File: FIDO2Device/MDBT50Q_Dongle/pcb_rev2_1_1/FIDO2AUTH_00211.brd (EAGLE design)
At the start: 22.9 x 38.7 mm, 35 parts, among them CN1 TE-1734028, CN2 IF_5PIN_H, CN3 IF_3PIN, SW1 SKRPACE010, SW2 SKTADAE010, U1 MDBT50Q-P1M, U2 XC6206P332MR-G, X1 NX3215SA-32.768K

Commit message: 回路図を修正
・ドキュメントタイトル修正、シート追加
・部品の小型化（リセット回路、差動信号回路、LED回路）
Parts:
- C5, C7, C8, C9: device Parts:C0603K -> Parts:C0402
- FB1, FB2, FB3: device Parts:C0402K@1 -> Parts:C0402
- R1, R2, R3, R4, R5, R6: device Parts:R0603 -> Parts:R0402

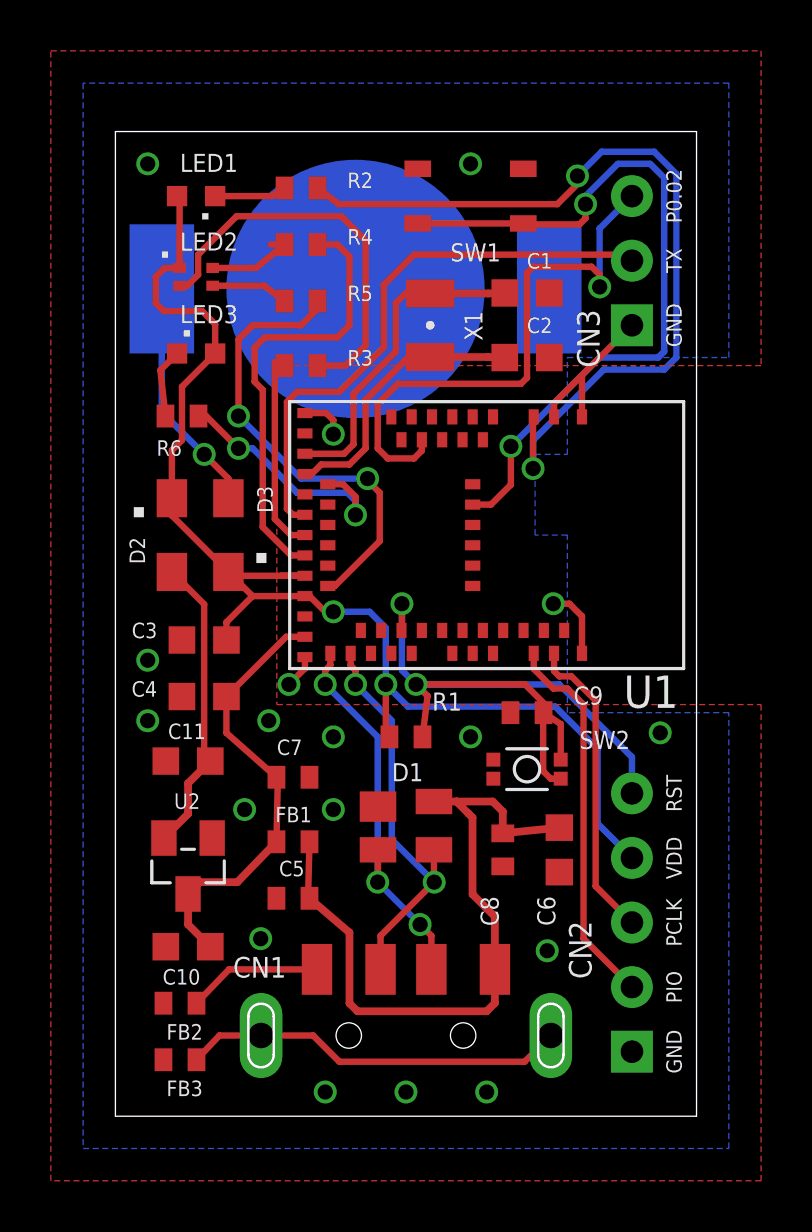
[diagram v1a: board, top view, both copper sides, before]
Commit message: 回路図を修正
・TWI_SDA、TWI_SCLを、実機動作確認結果を元に割り当て
・汎用I/Oを新規に２点割り当て
・プログラム用ピンの配置を修正
（RESETは不要なので廃止、VDDの位置をnRF52840 DK上の順列に合わせる）
・ERC、DRCともにOKを確認
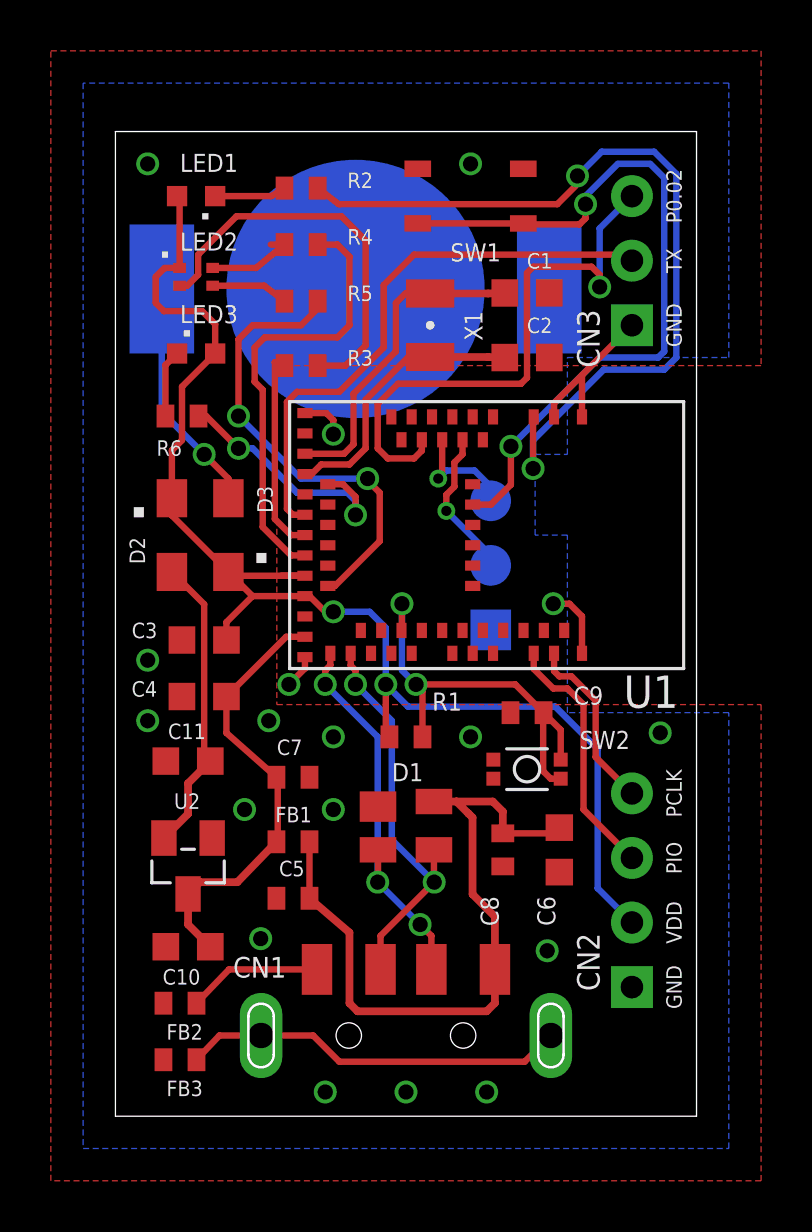
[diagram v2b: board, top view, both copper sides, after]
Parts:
- added CN4: IF_3PIN_SOL, Connectors:SOLPAD_3PIN
- CN2: value IF_5PIN_H -> IF_4PIN; device Connectors:HEADER_5PIN -> Connectors:HEADER_4PIN
- moved CN2 2.54 mm to (20.3, 5.08)
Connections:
- net AIN0 renamed TWI_SCL
- net UART_TX renamed TWI_SDA
- new net P0.03: CN4.3, U1.9
- new net P1.14: CN4.2, U1.7
- net 0V: now also CN4.1
- net RESET: no longer CN2.5
- net SWDCLK: now also CN2.4; no longer CN2.3
- net SWDIO: now also CN2.3; no longer CN2.2
- net VDD_NRF: now also CN2.2; no longer CN2.4
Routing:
- net RESET: track 29.1 -> 17.3 mm
- net P1.14: track 0.00 -> 5.93 mm, vias 0 -> 1
- net SWDIO: track 15.1 -> 9.98 mm
- net SWDCLK: track 12.1 -> 7.06 mm
- net P0.03: track 0.00 -> 4.61 mm, vias 0 -> 1
- net VDD_NRF: track 50.9 -> 53.5 mm
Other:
- board text removed: "RST"

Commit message: プリント基板設計データを修正
・ATECC608Aの配置前に、既存部品のレイアウトを修正
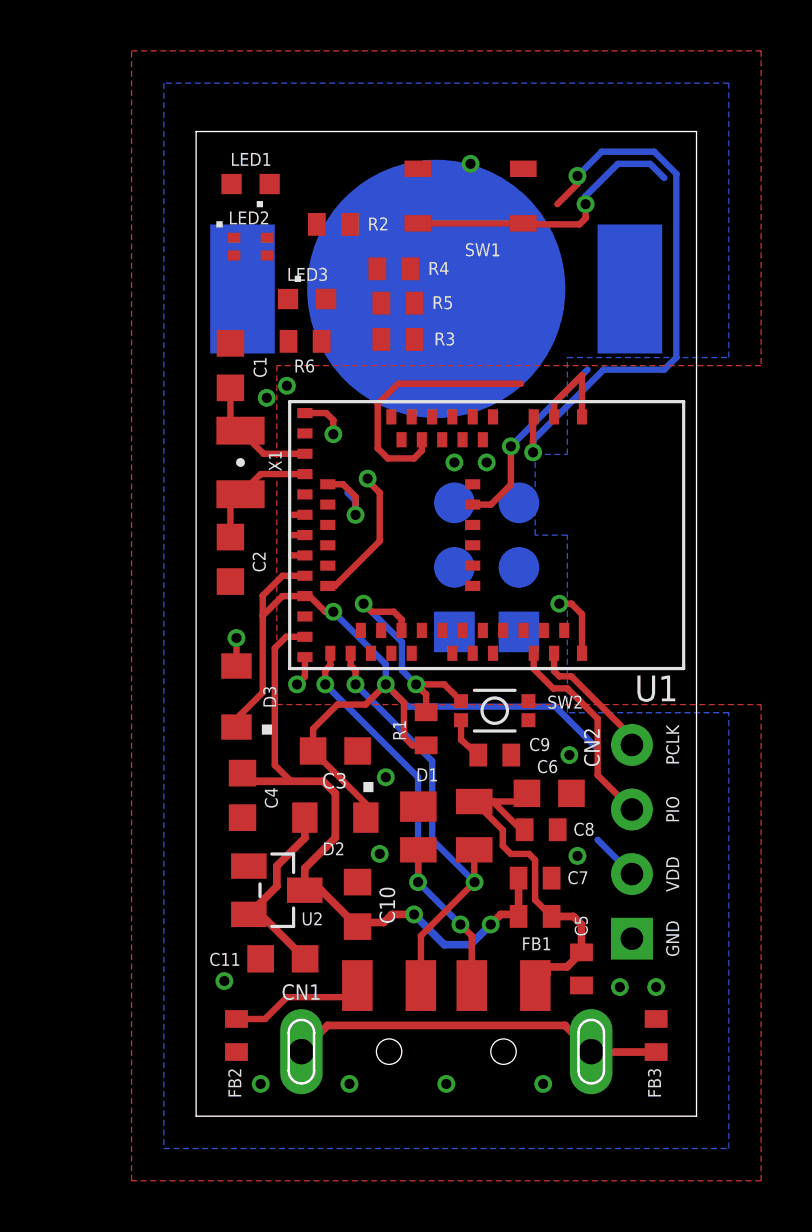
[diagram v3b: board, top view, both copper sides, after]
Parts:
- CN3: value IF_3PIN -> IF_3PIN_SOL; device Connectors:HEADER_3PIN -> Connectors:SOLPAD_3PIN
- moved FB3 18.8 mm to (21.3, 3.17), turned to 90 degrees
- moved C2 14.1 mm to (4.52, 21.9), turned to 270 degrees
- moved CN3 13.9 mm to (13.3, 19.1), flipped to the bottom
- moved D2 12.8 mm to (8.65, 11.7), turned to 180 degrees
- moved C1 12.0 mm to (4.52, 29.5), turned to 90 degrees
- moved C5 11.7 mm to (18.3, 5.79), turned to 270 degrees
- moved C7 10.3 mm to (16.5, 9.37)
- moved FB1 9.97 mm to (16.5, 7.86)
- moved X1 9.21 mm to (4.92, 25.7)
- moved C11 8.63 mm to (6.59, 6.19)
- moved C10 6.87 mm to (9.53, 8.33), turned to 90 degrees
- moved C3 6.76 mm to (8.65, 14.4), turned to 0 degrees
- moved D3 6.36 mm to (4.76, 16.5)
- moved R6 5.66 mm to (7.46, 30.5)
- moved LED3 4.86 mm to (7.54, 32.1)
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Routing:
- net TWI_SDA: track 22.5 -> 0.48 mm
- net LED2_G: track 17.6 -> 0.54 mm
- net VDD_NRF: track 53.5 -> 37.2 mm
- net N$1: track 15.7 -> 0.00 mm
- net LED2_B: track 18.7 -> 5.43 mm
- net VBUS: track 28.2 -> 15.8 mm
- net TWI_SCL: track 22.3 -> 10.2 mm, vias 1 -> 0
- net LED1: track 33.1 -> 22.2 mm
- net SW1: track 29.2 -> 19.0 mm
- net VBUS_NRF: track 17.5 -> 26.9 mm, vias 0 -> 2
- net N$5: track 9.32 -> 0.86 mm
- net XL1: track 12.8 -> 4.76 mm
- net LED2_R: track 8.02 -> 0.55 mm
- net LED3: track 10.1 -> 3.01 mm
- net XL2: track 10.9 -> 4.71 mm
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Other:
- board size 22.9 x 38.7 mm -> 19.7 x 38.7 mm
- board text removed: "P0.02"
- board text removed: "TX"

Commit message: プリント基板設計データを修正
・ATECC608Aの配置前の段階まで配線
・汎用I/Oを P0.25、P1.02 に変更
・TWI_SDA、TWI_SCL は表面に配置
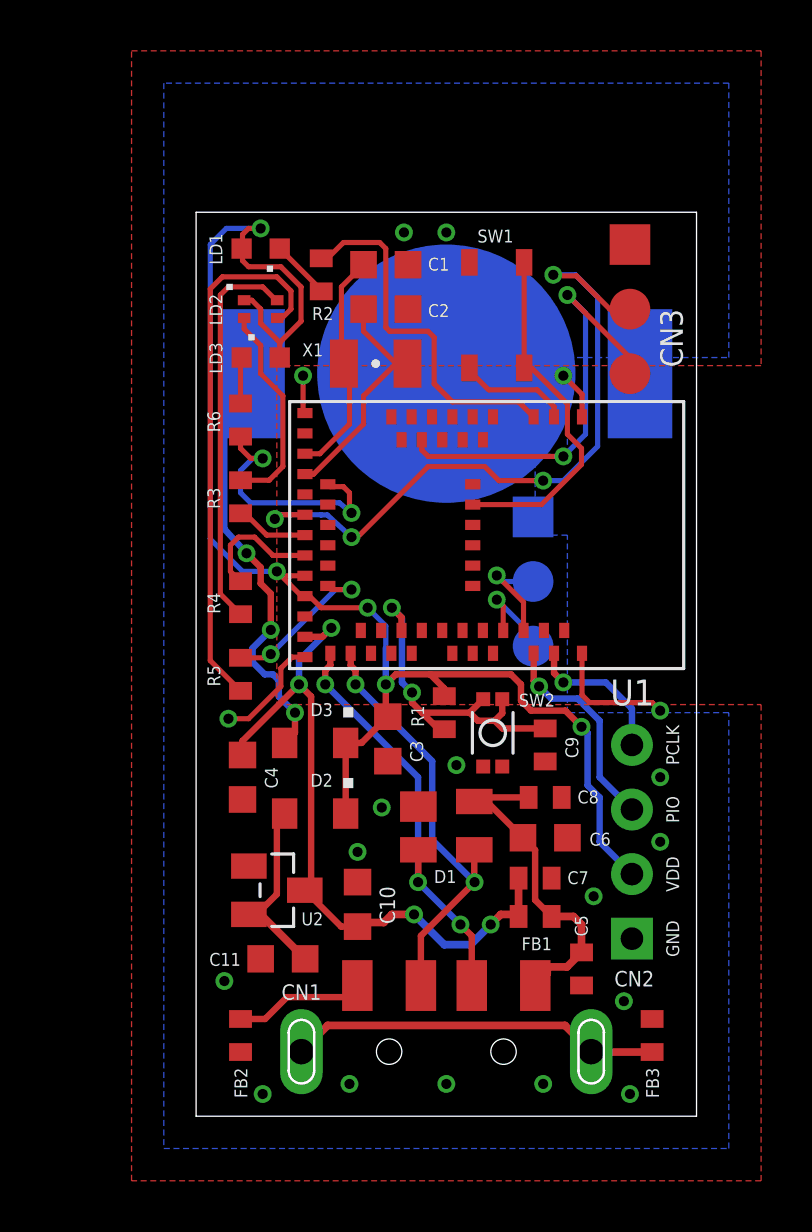
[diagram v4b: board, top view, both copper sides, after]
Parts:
- removed LED1: APHD1608LSURCK, Parts:CHIPLED_0603
- removed LED2: APHF1608LSEEQBDZGKC, Parts:APHF1608LSEEQBDZGKC
- removed LED3: APTD1608LSYCK, Parts:CHIPLED_0603
- added LD1: APHD1608LSURCK, Parts:CHIPLED_0603
- added LD2: APHF1608LSEEQBDZGKC, Parts:APHF1608LSEEQBDZGKC
- added LD3: APTD1608LSYCK, Parts:CHIPLED_0603
- moved CN3 16.7 mm to (20.2, 34.3), flipped to the top, turned to 270 degrees
- moved R5 15.9 mm to (4.92, 17.4), turned to 270 degrees
- moved R4 14.3 mm to (4.92, 20.4), turned to 270 degrees
- moved C2 11.6 mm to (10.6, 31.8), turned to 0 degrees
- moved R3 8.76 mm to (4.92, 24.4), turned to 90 degrees
- moved C1 7.29 mm to (10.6, 33.5), turned to 0 degrees
- moved X1 6.59 mm to (10.2, 29.6), turned to 0 degrees
- moved SW1 4.80 mm to (15.0, 31.5), turned to 270 degrees
- moved CN4 4.56 mm to (16.4, 23.6), turned to 270 degrees
- moved R6 4.00 mm to (4.92, 27.4), turned to 90 degrees
- moved D3 3.59 mm to (7.86, 14.7), turned to 180 degrees
- moved BAT1 3.36 mm to (13.0, 29.2)
- moved C3 2.12 mm to (10.7, 14.8), turned to 270 degrees
- moved R2 2.04 mm to (8.10, 33.1), turned to 270 degrees
- moved C9 2.02 mm to (16.9, 14.6), turned to 270 degrees
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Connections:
- removed net P0.03: CN4.3, U1.9
- removed net P1.14: CN4.2, U1.7
- new net P0.25: CN4.3, U1.49
- new net P1.02: CN4.2, U1.50
- net N$1: now also LD2.2; no longer LED2.2
- net N$11: now also LD1.C; no longer LED1.C
- net N$6: now also LD2.4; no longer LED2.4
- net N$7: now also LD2.3; no longer LED2.3
- net N$8: now also LD3.C; no longer LED3.C
- net VDD_NRF: now also LD1.A, LD2.1, LD3.A; no longer LED1.A, LED2.1, LED3.A
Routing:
- net TWI_SDA: track 0.48 -> 27.9 mm, vias 0 -> 4
- net VDD_NRF: track 37.2 -> 58.9 mm, vias 2 -> 5
- net N$7: track 0.00 -> 21.3 mm
- net N$5: track 0.86 -> 17.1 mm, vias 1 -> 3
- net N$6: track 0.00 -> 15.5 mm
- net N$1: track 0.00 -> 8.46 mm
- net 0V: track 9.33 -> 17.3 mm, vias 15 -> 19
- net LED1: track 22.2 -> 14.4 mm, vias 2 -> 0
- net TWI_SCL: track 10.2 -> 17.2 mm, vias 0 -> 2
- net LED3: track 3.01 -> 9.98 mm
- net SW1: track 19.0 -> 14.0 mm, vias 2 -> 0
- net XL2: track 4.71 -> 9.16 mm
- net LED2_G: track 0.54 -> 4.96 mm
- net XL1: track 4.76 -> 9.00 mm
- net P1.02: track 0.00 -> 4.13 mm, vias 0 -> 1
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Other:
- board size 19.7 x 38.7 mm -> 19.7 x 35.6 mm

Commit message: プリント基板設計データを修正
・汎用I/OブレイクアウトからGNDを削除（不要なため）
・GNDパターンを改善
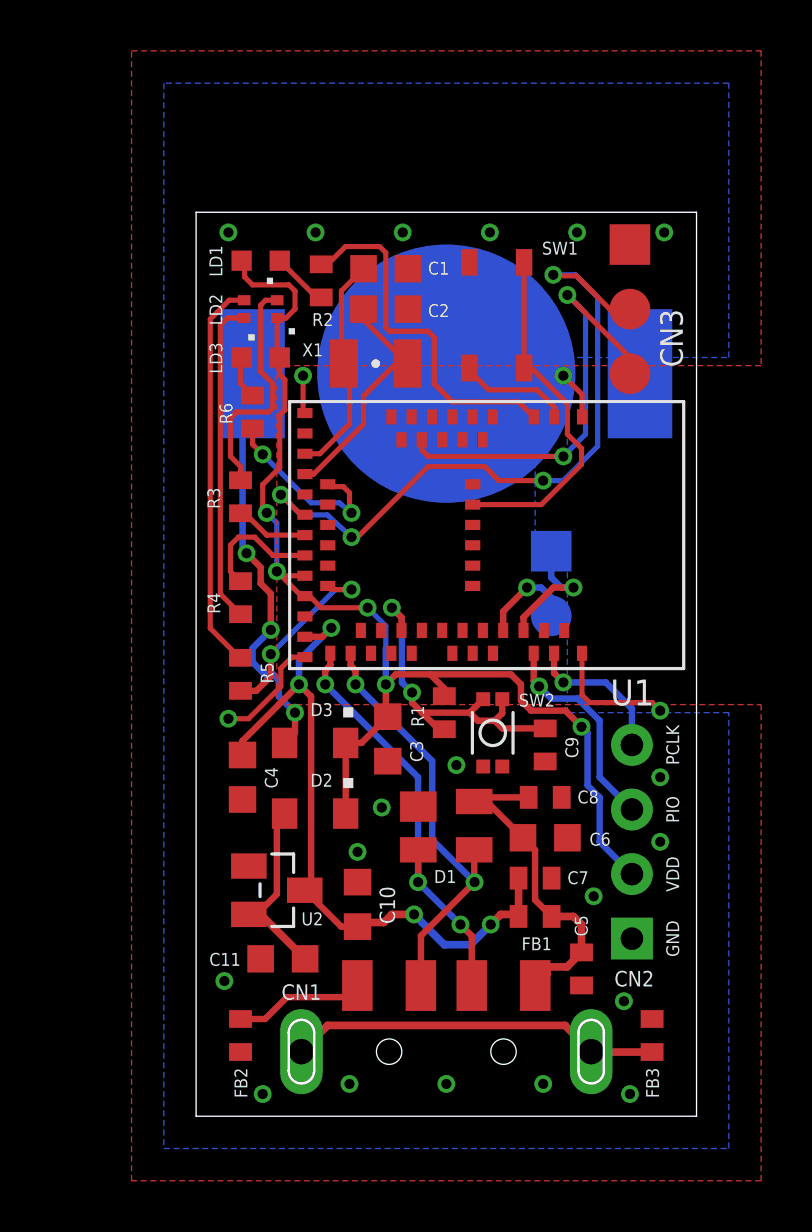
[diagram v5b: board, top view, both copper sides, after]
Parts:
- removed CN4: IF_3PIN_SOL, Connectors:SOLPAD_3PIN
- added CN5: IF_2PIN_SOL, Connectors:SOLPAD_2PIN
- moved R6 0.57 mm to (5.40, 27.7)
- moved LD1 0.48 mm to (5.71, 33.7)
- moved R2 0.24 mm to (8.10, 32.9)
- moved C1 0.16 mm to (10.6, 33.3)
- turned LD2 to 180 degrees
- turned R5 to 90 degrees
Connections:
- net 0V: no longer CN4.1
- net P0.25: now also CN5.2; no longer CN4.3
- net P1.02: now also CN5.1; no longer CN4.2
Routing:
- net VDD_NRF: track 58.9 -> 46.9 mm
- net N$7: track 21.3 -> 15.5 mm
- net N$6: track 15.5 -> 12.7 mm
- net LED3: track 9.98 -> 7.47 mm
- net LED2_B: track 6.49 -> 7.54 mm
- net N$1: track 8.46 -> 9.42 mm
- net P1.02: track 4.13 -> 5.03 mm
- net P0.25: track 3.73 -> 4.54 mm
- net N$5: track 17.1 -> 16.5 mm
- net 0V: vias 19 -> 23
